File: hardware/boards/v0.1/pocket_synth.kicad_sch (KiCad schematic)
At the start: 6 parts

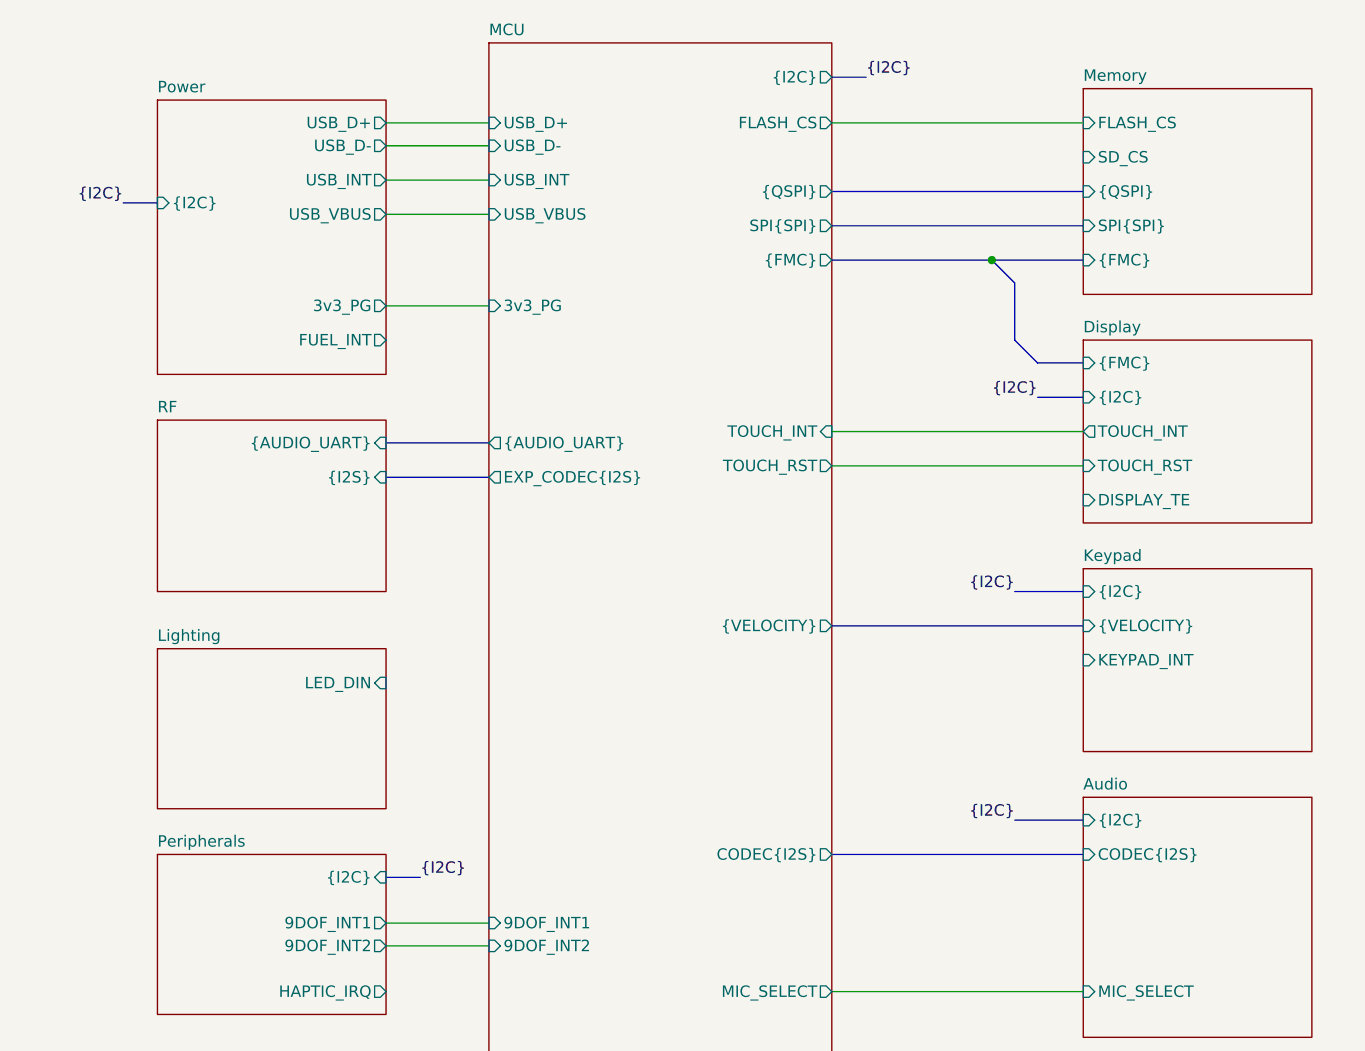
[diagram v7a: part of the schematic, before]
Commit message: feat: route dedicated audio I2C bus
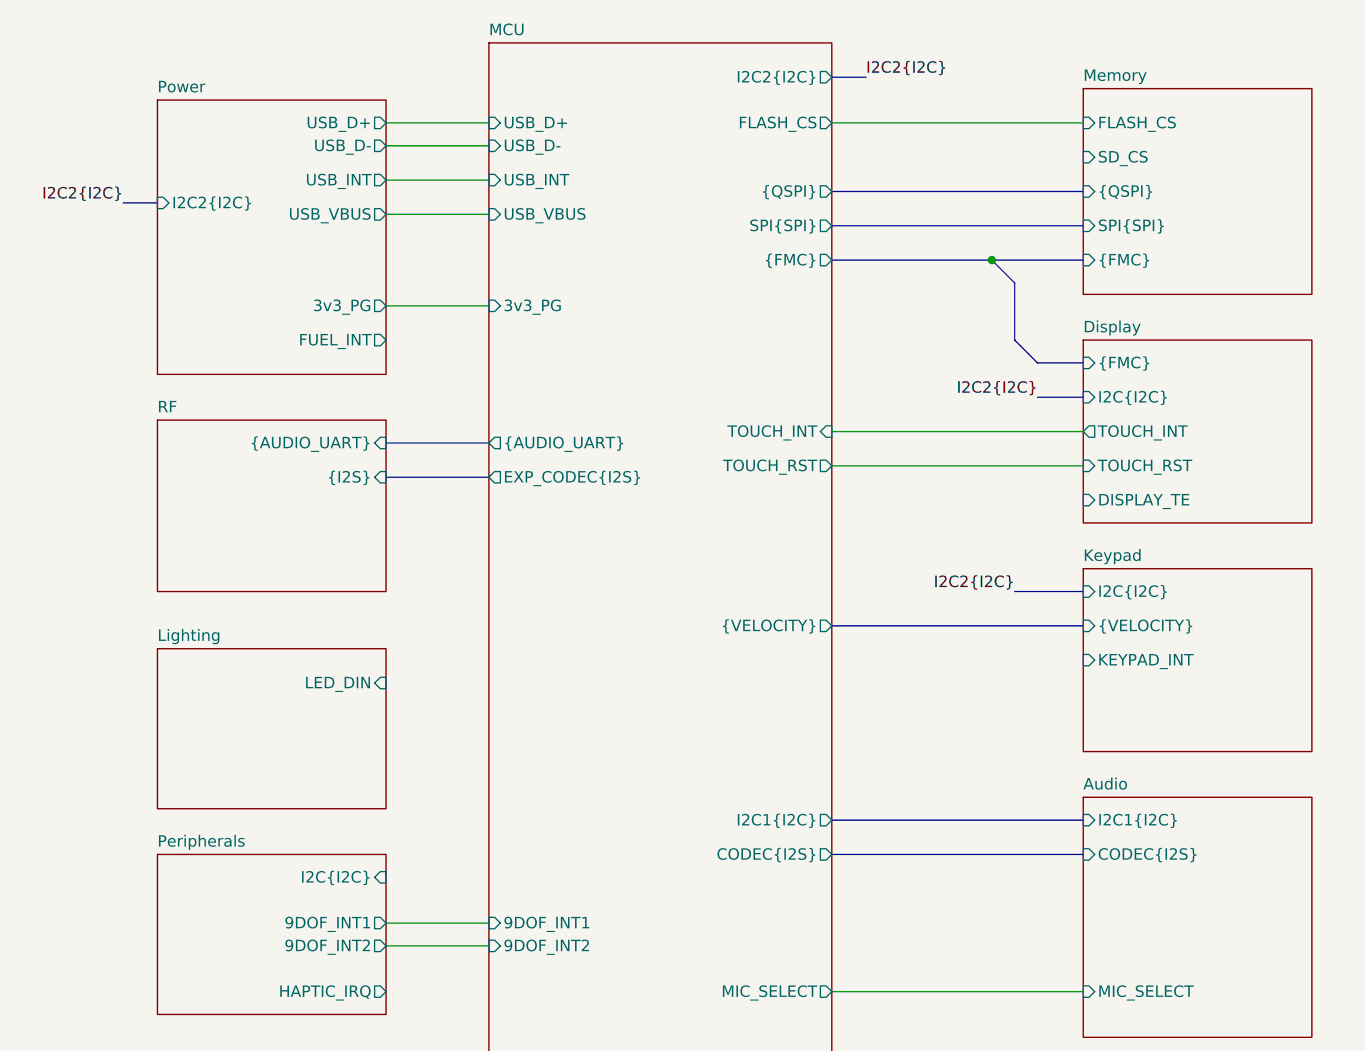
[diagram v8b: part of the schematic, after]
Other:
- sheet Audio ports: added I2C1{I2C}; removed {I2C}
- sheet Display ports: added I2C{I2C}; removed {I2C}
- sheet Keypad ports: added I2C{I2C}; removed {I2C}
- sheet MCU ports: added I2C1{I2C}, I2C2{I2C}; removed {I2C}
- sheet Peripherals ports: added I2C{I2C}; removed {I2C}
- sheet Power ports: added I2C2{I2C}; removed {I2C}
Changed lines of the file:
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@@
+		)
+	)
+	(wire
+		(pts
+			(xy 29.21 185.42) (xy 29.21 187.96)
+		)
+		(stroke
+			(width 0)
+			(type default)
+		)
+	)
+	(wire
+		(pts
+			(xy 69.85 175.26) (xy 67.31 175.26)
+		)
+		(stroke
+			(width 0)
+			(type default)
 		)
 	)
 	(bus
 		(pts
-			(xy 121.92 106.68) (xy 129.54 106.68)
+			(xy 124.46 55.88) (xy 129.54 55.88)
 		)
 		(stroke
@@
 	(wire
 		(pts
-			(xy 29.21 185.42) (xy 29.21 187.96)
+			(xy 52.07 31.75) (xy 63.5 31.75)
 		)
 		(stroke
@@
 	(wire
 		(pts
-			(xy 69.85 175.26) (xy 67.31 175.26)
+			(xy 52.07 49.53) (xy 63.5 49.53)
 		)
 		(stroke
@@
 	(bus
 		(pts
-			(xy 124.46 55.88) (xy 129.54 55.88)
+			(xy 121.92 53.34) (xy 124.46 55.88)
 		)
 		(stroke
@@
 	(wire
 		(pts
-			(xy 52.07 31.75) (xy 63.5 31.75)
+			(xy 38.1 185.42) (xy 38.1 187.96)
 		)
 		(stroke
@@
 	(wire
 		(pts
-			(xy 52.07 49.53) (xy 63.5 49.53)
+			(xy 52.07 118.11) (xy 63.5 118.11)
+		)
+		(stroke
+			(width 0)
+			(type default)
+		)
+	)
+	(wire
+		(pts
+			(xy 101.6 125.73) (xy 129.54 125.73)
 		)
 		(stroke
@@
 	(bus
 		(pts
-			(xy 121.92 53.34) (xy 124.46 55.88)
+			(xy 101.6 36.83) (xy 129.54 36.83)
 		)
 		(stroke
@@
 	(wire
 		(pts
-			(xy 38.1 185.42) (xy 38.1 187.96)
-		)
-		(stroke
-			(width 0)
-			(type default)
-		)
-	)
-	(wire
-		(pts
-			(xy 52.07 118.11) (xy 63.5 118.11)
-		)
-		(stroke
-			(width 0)
-			(type default)
-		)
-	)
-	(wire
-		(pts
-			(xy 101.6 125.73) (xy 129.54 125.73)
-		)
-		(stroke
-			(width 0)
-			(type default)
-		)
-	)
-	(bus
-		(pts
-			(xy 101.6 36.83) (xy 129.54 36.83)
-		)
-		(stroke
-			(width 0)
-			(type default)
-		)
-	)
-	(wire
-		(pts
 			(xy 69.85 187.96) (xy 67.31 187.96)
-		)
-		(stroke
-			(width 0)
-			(type default)
-		)
-	)
-	(bus
-		(pts
-			(xy 55.88 113.03) (xy 52.07 113.03)
 		)
 		(stroke
@@
 		)
 	)
+	(bus
+		(pts
+			(xy 101.6 106.68) (xy 129.54 106.68)
+		)
+		(stroke
+			(width 0)
+			(type default)
+		)
+	)
 	(wire
 		(pts
@@
 		)
 	)
-	(label "{I2C}"
+	(label "I2C2{I2C}"
 		(at 121.92 81.28 180)
 		(effects
@@
 		)
 	)
-	(label "{I2C}"
-		(at 121.92 106.68 180)
-		(effects
-			(font
-				(size 1.27 1.27)
-				(thickness 0.1588)
-			)
-			(justify right bottom)
-		)
-	)
-	(label "{I2C}"
+	(label "I2C2{I2C}"
 		(at 124.46 59.69 180)
 		(effects
@@
 		)
 	)
-	(label "{I2C}"
+	(label "I2C2{I2C}"
 		(at 22.86 38.1 180)
 		(effects
@@
 		)
 	)
-	(label "{I2C}"
+	(label "I2C2{I2C}"
 		(at 105.41 24.13 0)
-		(effects
-			(font
-				(size 1.27 1.27)
-				(thickness 0.1588)
-			)
-			(justify left bottom)
-		)
-	)
-	(label "{I2C}"
-		(at 55.88 113.03 0)
 		(effects
 			(font
@@
 			)
 		)
-		(pin "{I2C}" output
+		(pin "I2C2{I2C}" output
 			(at 101.6 24.13 0)
 			(effects
@@
 				)
 				(justify left)
+			)
+		)
+		(pin "I2C1{I2C}" output
+			(at 101.6 106.68 0)
+			(effects
+				(font
+					(size 1.27 1.27)
+				)
+				(justify right)
 			)
 		)
@@
 			)
 		)
-		(pin "{I2C}" input
+		(pin "I2C2{I2C}" input
 			(at 26.67 38.1 180)
 			(effects
@@
 			)
 		)
-		(pin "{I2C}" input
+		(pin "I2C{I2C}" input
 			(at 129.54 81.28 180)
 			(effects
@@
 			)
 		)
-		(pin "{I2C}" input
+		(pin "I2C1{I2C}" input
 			(at 129.54 106.68 180)
 			(effects
@@
 			)
 		)
-		(pin "{I2C}" input
+		(pin "I2C{I2C}" input
 			(at 129.54 59.69 180)
 			(effects
@@
 			)
 		)
-		(pin "{I2C}" input
+		(pin "I2C{I2C}" input
 			(at 52.07 113.03 0)
 			(effects
